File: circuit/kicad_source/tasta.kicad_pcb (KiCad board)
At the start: 2 copper layers, 30.5 x 47 mm, 15 parts, among them IC1 ATTINY85-P, J1 USB, K1 CONN_3, SW1 SW_PUSH, SW2 SW_PUSH

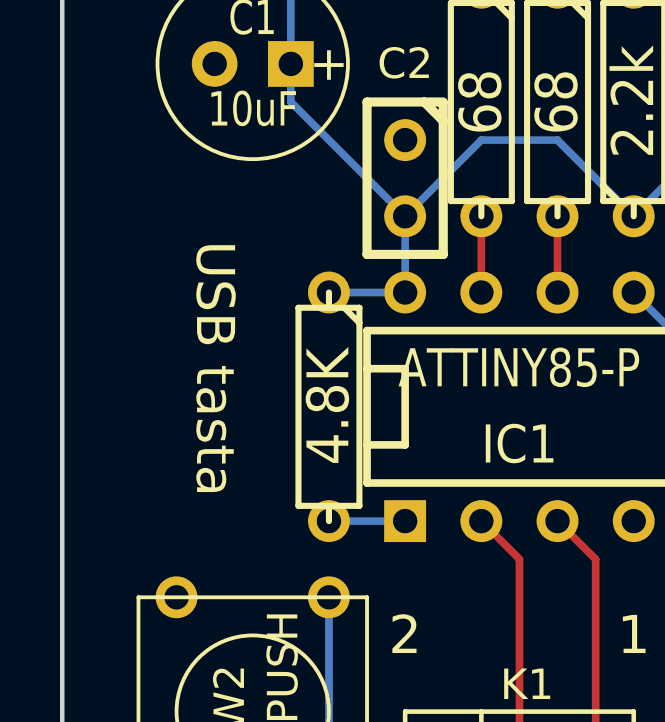
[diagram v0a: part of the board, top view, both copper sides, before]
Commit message: add logo to PCB
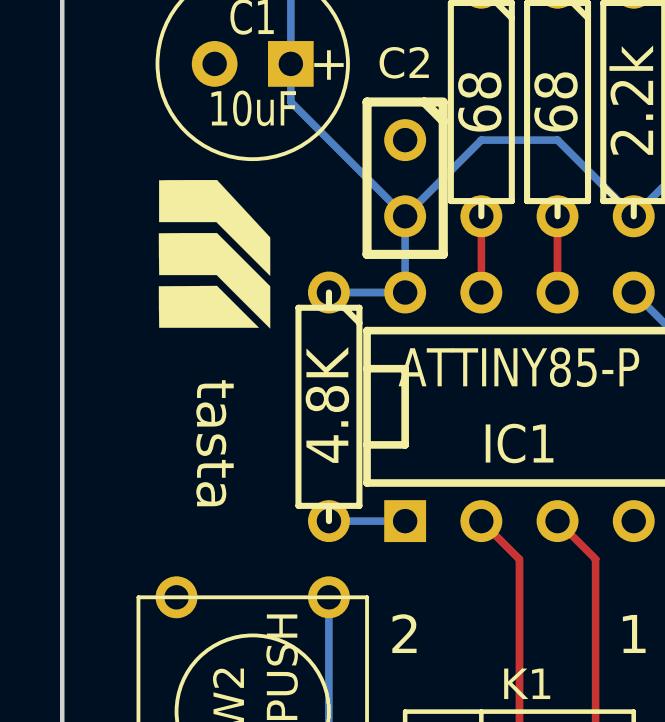
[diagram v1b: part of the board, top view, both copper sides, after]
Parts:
- added VAL: REF, mmitch_logo_front, F.Cu at (64.8, 76.2)
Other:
- board text added: "tasta"
- board text removed: "USB tasta"
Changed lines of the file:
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@@
     (tracks 42)
     (zones 0)
-    (modules 15)
+    (modules 16)
     (nets 12)
   )
@@
     (visible_elements FFFFFFBF)
     (pcbplotparams
-      (layerselection 3178497)
+      (layerselection 284196865)
       (usegerberextensions true)
       (excludeedgelayer true)
@@
       (plotinvisibletext false)
       (padsonsilk false)
-      (subtractmaskfromsilk false)
+      (subtractmaskfromsilk true)
       (outputformat 1)
       (mirror false)
-      (drillshape 1)
+      (drillshape 0)
       (scaleselection 1)
-      (outputdirectory ""))
+      (outputdirectory /tmp))
   )
   (net 0 "")
@@
     (add_net N-000006)
   )
+  (module mmitch_logo_front (layer F.Cu)
+    (at 64.77 76.2 270)
+    (solder_mask_margin 0.15)
+    (zone_connect 2)
+    (fp_text reference VAL (at 0 0 270) (layer F.SilkS) hide
+      (effects (font (size 0.381 0.381) (thickness 0.127)))
+    )
+    (fp_text value REF (at 0 0 270) (layer F.SilkS) hide
+      (effects (font (size 0.381 0.381) (thickness 0.127)))
+    )
+    (fp_poly (pts (xy 2.47396 -1.85166) (xy 1.58242 -0.95758) (xy 0.68834 -0.06604) (xy 0.68834 0.89154)
+      (xy 0.68834 1.84912) (xy 0.23622 1.8542) (xy 0.15494 1.8542) (xy 0.07112 1.85674)
+      (xy -0.01524 1.85674) (xy -0.09906 1.85674) (xy -0.18288 1.85674) (xy -0.25908 1.85674)
+      (xy -0.3302 1.85928) (xy -0.3937 1.85928) (xy -0.4445 1.85928) (xy -0.45974 1.85928)
+      (xy -0.70358 1.85928) (xy -0.70866 1.41732) (xy -0.70866 1.33604) (xy -0.70866 1.2446)
+      (xy -0.7112 1.14554) (xy -0.7112 1.0414) (xy -0.7112 0.93218) (xy -0.7112 0.82296)
+      (xy -0.7112 0.71374) (xy -0.7112 0.6096) (xy -0.7112 0.51054) (xy -0.7112 0.44958)
+      (xy -0.7112 -0.07874) (xy 0.17526 -0.9652) (xy 1.06172 -1.85166) (xy 1.76784 -1.85166)
+      (xy 2.47396 -1.85166) (xy 2.47396 -1.85166)) (layer F.SilkS) (width 0.00254))
+    (fp_poly (pts (xy 2.44602 1.84912) (xy 1.99898 1.8542) (xy 1.9177 1.8542) (xy 1.83388 1.85674)
+      (xy 1.74752 1.85674) (xy 1.6637 1.85674) (xy 1.58242 1.85674) (xy 1.50368 1.85674)
+      (xy 1.43256 1.85928) (xy 1.3716 1.85928) (xy 1.31826 1.85928) (xy 1.3081 1.85928)
+      (xy 1.06172 1.85928) (xy 1.05664 1.17348) (xy 1.05664 1.07442) (xy 1.05664 0.97536)
+      (xy 1.05664 0.8763) (xy 1.0541 0.77724) (xy 1.0541 0.68072) (xy 1.0541 0.58928)
+      (xy 1.0541 0.50292) (xy 1.05156 0.42164) (xy 1.05156 0.35052) (xy 1.05156 0.28702)
+      (xy 1.05156 0.23368) (xy 1.05156 0.2032) (xy 1.04902 -0.07874) (xy 1.74752 -0.77724)
+      (xy 2.44602 -1.47828) (xy 2.44602 0.18542) (xy 2.44602 1.84912) (xy 2.44602 1.84912)) (layer F.SilkS) (width 0.00254))
+    (fp_poly (pts (xy 0.71628 -1.85166) (xy -0.18034 -0.95504) (xy -1.07696 -0.05842) (xy -1.07696 0.89662)
+      (xy -1.07696 1.85166) (xy -1.77292 1.85166) (xy -2.46888 1.85166) (xy -2.47396 1.67386)
+      (xy -2.47396 1.64592) (xy -2.47396 1.60528) (xy -2.4765 1.55448) (xy -2.4765 1.49352)
+      (xy -2.4765 1.42494) (xy -2.4765 1.34874) (xy -2.4765 1.26746) (xy -2.4765 1.17856)
+      (xy -2.4765 1.08458) (xy -2.47904 0.98806) (xy -2.47904 0.889) (xy -2.47904 0.7874)
+      (xy -2.47904 0.70866) (xy -2.47904 -0.07874) (xy -1.524 -0.9652) (xy -0.56642 -1.85166)
+      (xy 0.07366 -1.85166) (xy 0.71628 -1.85166) (xy 0.71628 -1.85166)) (layer F.SilkS) (width 0.00254))
+  )
   (module C1V7 (layer F.Cu)
     (at 66.04 69.85 180)
@@
   (gr_line (start 90.17 97.79) (end 90.17 50.8) (angle 90) (layer Edge.Cuts) (width 0.15))
   (gr_line (start 59.69 97.79) (end 90.17 97.79) (angle 90) (layer Edge.Cuts) (width 0.15))
-  (gr_text "USB tasta\n" (at 64.77 80.01 270) (layer F.SilkS)
+  (gr_text "tasta\n" (at 64.77 82.55 270) (layer F.SilkS)
     (effects (font (size 1.27 1.27) (thickness 0.3)))
   )

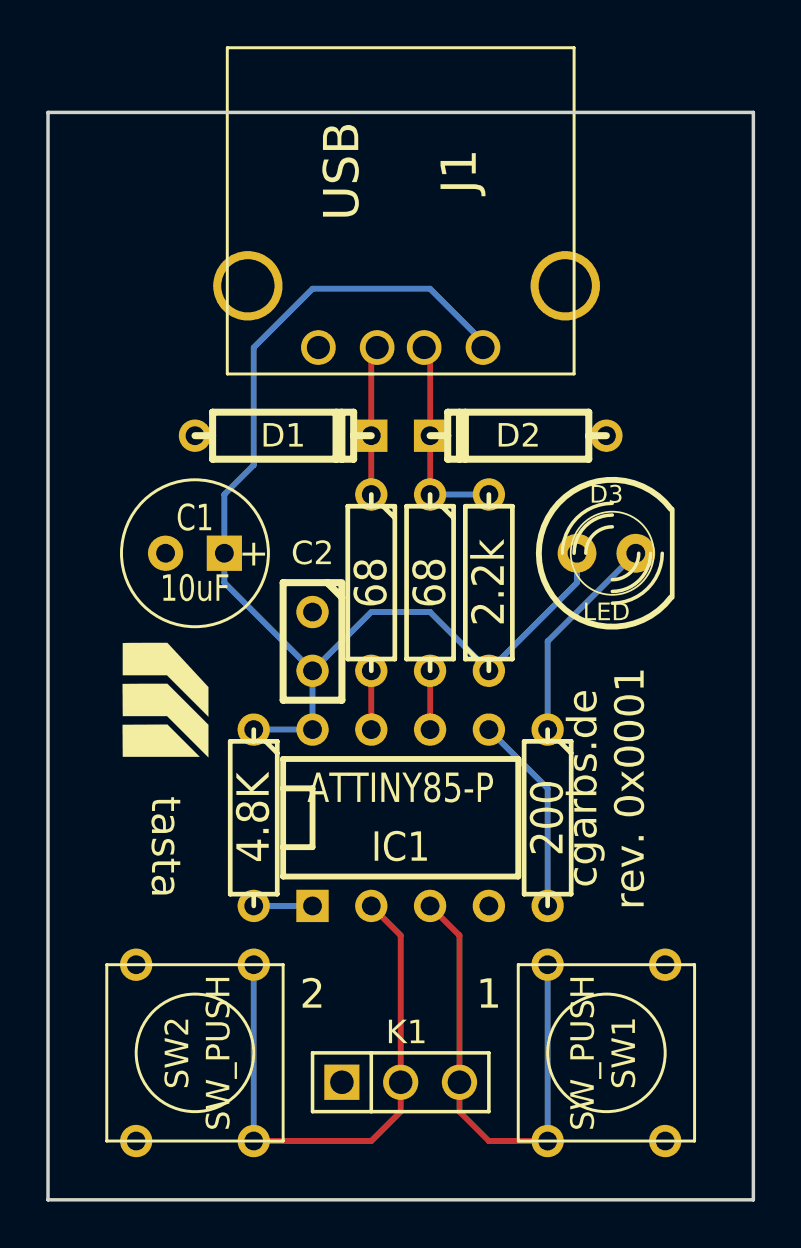
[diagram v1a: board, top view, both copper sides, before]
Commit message: update logo on PCB
handcrafted logo is better than Bitmap2Component conversion
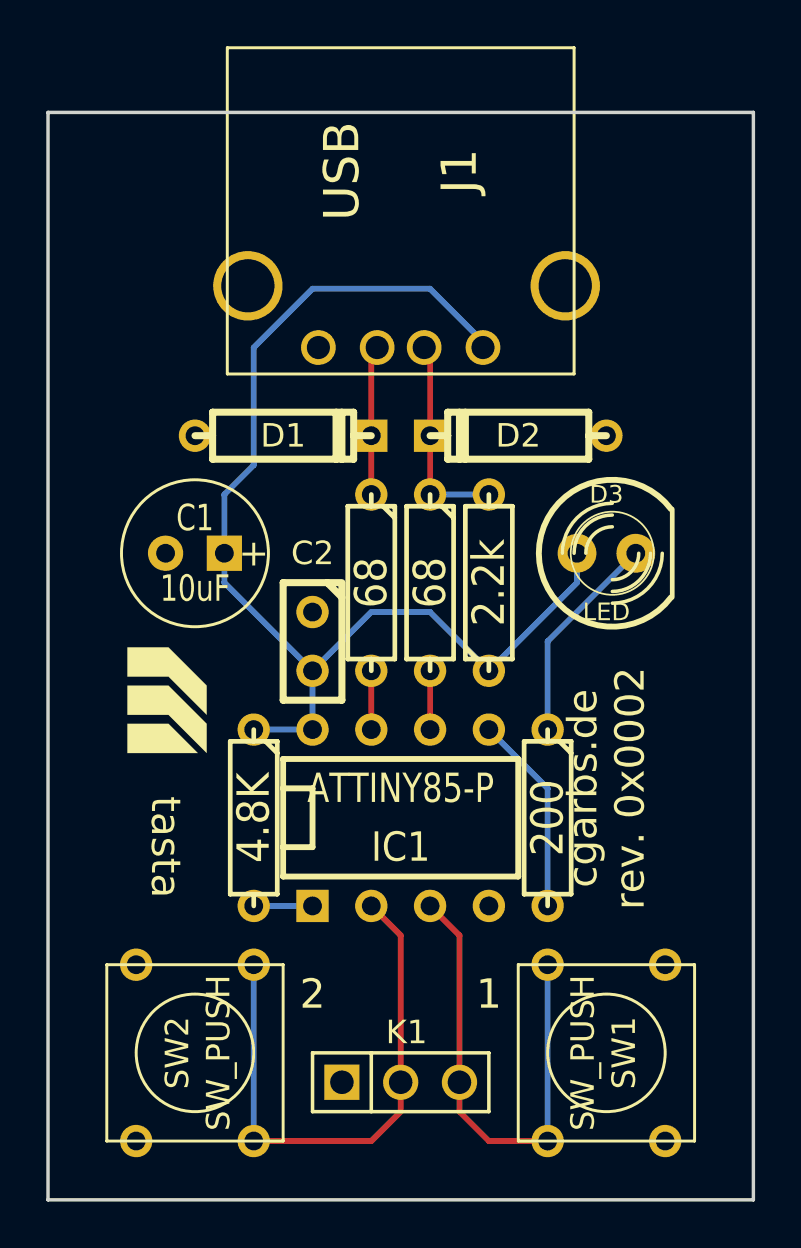
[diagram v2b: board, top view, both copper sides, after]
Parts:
- removed VAL: REF, mmitch_logo_front
- added ?: , mmitch_logo_back_silk, F.Cu at (64.8, 76.2)
- added ?: , mmitch_logo_front_silk, F.Cu at (64.8, 76.2)
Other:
- board text added: "cgarbs.de rev. 0x0002"
- board text removed: "cgarbs.de rev. 0x0001"
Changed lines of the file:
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@@
     (tracks 42)
     (zones 0)
-    (modules 16)
+    (modules 17)
     (nets 12)
   )
@@
     (add_net N-000006)
   )
-  (module mmitch_logo_front (layer F.Cu)
-    (at 64.77 76.2 270)
-    (solder_mask_margin 0.15)
-    (zone_connect 2)
-    (fp_text reference VAL (at 0 0 270) (layer F.SilkS) hide
-      (effects (font (size 0.381 0.381) (thickness 0.127)))
-    )
-    (fp_text value REF (at 0 0 270) (layer F.SilkS) hide
-      (effects (font (size 0.381 0.381) (thickness 0.127)))
-    )
-    (fp_poly (pts (xy 2.47396 -1.85166) (xy 1.58242 -0.95758) (xy 0.68834 -0.06604) (xy 0.68834 0.89154)
-      (xy 0.68834 1.84912) (xy 0.23622 1.8542) (xy 0.15494 1.8542) (xy 0.07112 1.85674)
-      (xy -0.01524 1.85674) (xy -0.09906 1.85674) (xy -0.18288 1.85674) (xy -0.25908 1.85674)
-      (xy -0.3302 1.85928) (xy -0.3937 1.85928) (xy -0.4445 1.85928) (xy -0.45974 1.85928)
-      (xy -0.70358 1.85928) (xy -0.70866 1.41732) (xy -0.70866 1.33604) (xy -0.70866 1.2446)
-      (xy -0.7112 1.14554) (xy -0.7112 1.0414) (xy -0.7112 0.93218) (xy -0.7112 0.82296)
-      (xy -0.7112 0.71374) (xy -0.7112 0.6096) (xy -0.7112 0.51054) (xy -0.7112 0.44958)
-      (xy -0.7112 -0.07874) (xy 0.17526 -0.9652) (xy 1.06172 -1.85166) (xy 1.76784 -1.85166)
-      (xy 2.47396 -1.85166) (xy 2.47396 -1.85166)) (layer F.SilkS) (width 0.00254))
-    (fp_poly (pts (xy 2.44602 1.84912) (xy 1.99898 1.8542) (xy 1.9177 1.8542) (xy 1.83388 1.85674)
-      (xy 1.74752 1.85674) (xy 1.6637 1.85674) (xy 1.58242 1.85674) (xy 1.50368 1.85674)
-      (xy 1.43256 1.85928) (xy 1.3716 1.85928) (xy 1.31826 1.85928) (xy 1.3081 1.85928)
-      (xy 1.06172 1.85928) (xy 1.05664 1.17348) (xy 1.05664 1.07442) (xy 1.05664 0.97536)
-      (xy 1.05664 0.8763) (xy 1.0541 0.77724) (xy 1.0541 0.68072) (xy 1.0541 0.58928)
-      (xy 1.0541 0.50292) (xy 1.05156 0.42164) (xy 1.05156 0.35052) (xy 1.05156 0.28702)
-      (xy 1.05156 0.23368) (xy 1.05156 0.2032) (xy 1.04902 -0.07874) (xy 1.74752 -0.77724)
-      (xy 2.44602 -1.47828) (xy 2.44602 0.18542) (xy 2.44602 1.84912) (xy 2.44602 1.84912)) (layer F.SilkS) (width 0.00254))
-    (fp_poly (pts (xy 0.71628 -1.85166) (xy -0.18034 -0.95504) (xy -1.07696 -0.05842) (xy -1.07696 0.89662)
-      (xy -1.07696 1.85166) (xy -1.77292 1.85166) (xy -2.46888 1.85166) (xy -2.47396 1.67386)
-      (xy -2.47396 1.64592) (xy -2.47396 1.60528) (xy -2.4765 1.55448) (xy -2.4765 1.49352)
-      (xy -2.4765 1.42494) (xy -2.4765 1.34874) (xy -2.4765 1.26746) (xy -2.4765 1.17856)
-      (xy -2.4765 1.08458) (xy -2.47904 0.98806) (xy -2.47904 0.889) (xy -2.47904 0.7874)
-      (xy -2.47904 0.70866) (xy -2.47904 -0.07874) (xy -1.524 -0.9652) (xy -0.56642 -1.85166)
-      (xy 0.07366 -1.85166) (xy 0.71628 -1.85166) (xy 0.71628 -1.85166)) (layer F.SilkS) (width 0.00254))
-  )
   (module C1V7 (layer F.Cu)
     (at 66.04 69.85 180)
@@
     )
   )
+  (module mmitch_logo_back_silk (layer F.Cu)
+    (at 64.77 76.2 90)
+    (fp_text reference "" (at 0 0 90) (layer F.SilkS)
+      (effects (font (size 1.524 1.524) (thickness 0.15)))
+    )
+    (fp_text value "" (at 0 0 90) (layer F.SilkS)
+      (effects (font (size 1.524 1.524) (thickness 0.15)))
+    )
+    (fp_poly (pts (xy -0.635 -1.778) (xy 1.016 -0.127) (xy 1.016 1.651) (xy 2.286 1.651)
+      (xy 2.286 -0.127) (xy 0.635 -1.778)) (layer B.SilkS) (width 0.00254))
+    (fp_poly (pts (xy 0.635 1.651) (xy -0.635 1.651) (xy -0.635 -0.127) (xy -2.286 -1.778)
+      (xy -1.016 -1.778) (xy 0.635 -0.127)) (layer B.SilkS) (width 0.00254))
+    (fp_poly (pts (xy -1.016 1.651) (xy -2.286 1.651) (xy -2.286 -1.397) (xy -1.016 -0.127)) (layer B.SilkS) (width 0.00254))
+  )
+  (module mmitch_logo_front_silk (layer F.Cu)
+    (at 64.77 76.2 270)
+    (fp_text reference "" (at 0 0 270) (layer F.SilkS)
+      (effects (font (size 1.524 1.524) (thickness 0.15)))
+    )
+    (fp_text value "" (at 0 0 270) (layer F.SilkS)
+      (effects (font (size 1.524 1.524) (thickness 0.15)))
+    )
+    (fp_poly (pts (xy 0.635 -1.778) (xy -1.016 -0.127) (xy -1.016 1.651) (xy -2.286 1.651)
+      (xy -2.286 -0.127) (xy -0.635 -1.778)) (layer F.SilkS) (width 0.00254))
+    (fp_poly (pts (xy -0.635 1.651) (xy 0.635 1.651) (xy 0.635 -0.127) (xy 2.286 -1.778)
+      (xy 1.016 -1.778) (xy -0.635 -0.127)) (layer F.SilkS) (width 0.00254))
+    (fp_poly (pts (xy 1.016 1.651) (xy 2.286 1.651) (xy 2.286 -1.397) (xy 1.016 -0.127)) (layer F.SilkS) (width 0.00254))
+  )
   (gr_text 1 (at 78.74 88.9) (layer F.SilkS)
     (effects (font (size 1.27 1.27) (thickness 0.3)))
@@
     (effects (font (size 1.27 1.27) (thickness 0.3)))
   )
-  (gr_text "cgarbs.de\nrev. 0x0001\n" (at 83.82 80.01 90) (layer F.SilkS)
+  (gr_text "cgarbs.de\nrev. 0x0002\n" (at 83.82 80.01 90) (layer F.SilkS)
     (effects (font (size 1.27 1.27) (thickness 0.3)))
   )

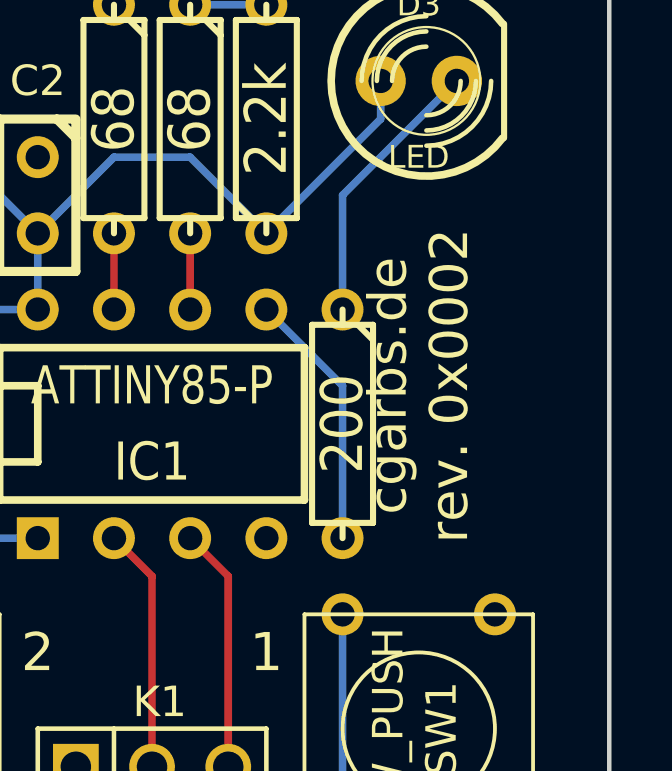
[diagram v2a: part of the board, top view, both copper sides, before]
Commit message: update revision after frontsilk extension change
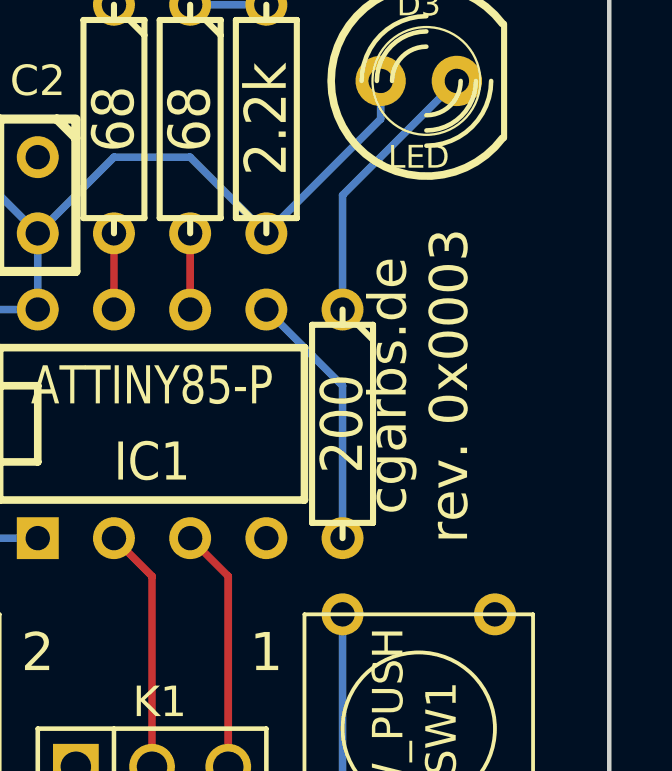
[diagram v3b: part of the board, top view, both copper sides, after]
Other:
- board text added: "cgarbs.de rev. 0x0003"
- board text removed: "cgarbs.de rev. 0x0002"
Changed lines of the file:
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@@
       (drillshape 0)
       (scaleselection 1)
-      (outputdirectory /tmp))
+      (outputdirectory ../kicad_export/))
   )
   (net 0 "")
@@
     (effects (font (size 1.27 1.27) (thickness 0.3)))
   )
-  (gr_text "cgarbs.de\nrev. 0x0002\n" (at 83.82 80.01 90) (layer F.SilkS)
+  (gr_text "cgarbs.de\nrev. 0x0003\n" (at 83.82 80.01 90) (layer F.SilkS)
     (effects (font (size 1.27 1.27) (thickness 0.3)))
   )
